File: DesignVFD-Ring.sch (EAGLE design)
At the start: 5 parts, among them J1 NPPN081BFLD-RC, J2 NPPN081BFLD-RC, J3 NPPN081BFLD-RC, J4 NPPN081BFLD-RC

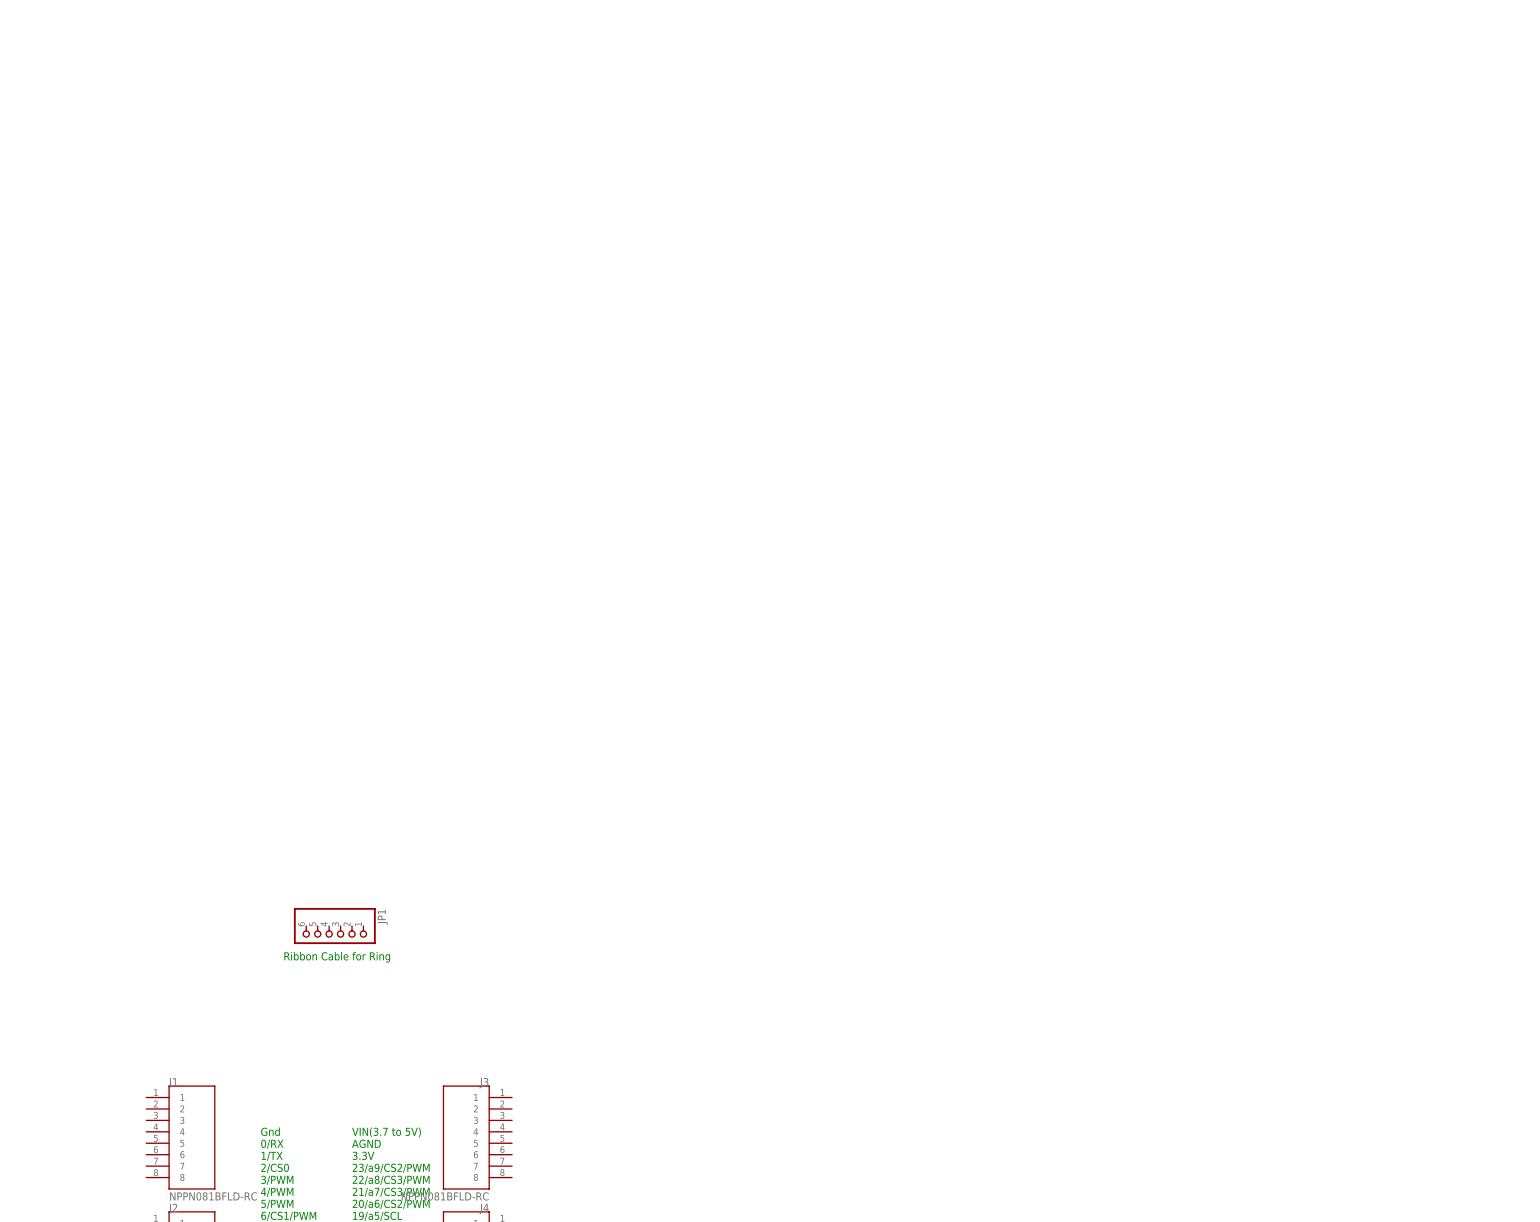
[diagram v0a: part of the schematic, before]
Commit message: downloaded some spreadsheets, added most parts, finished ignition input
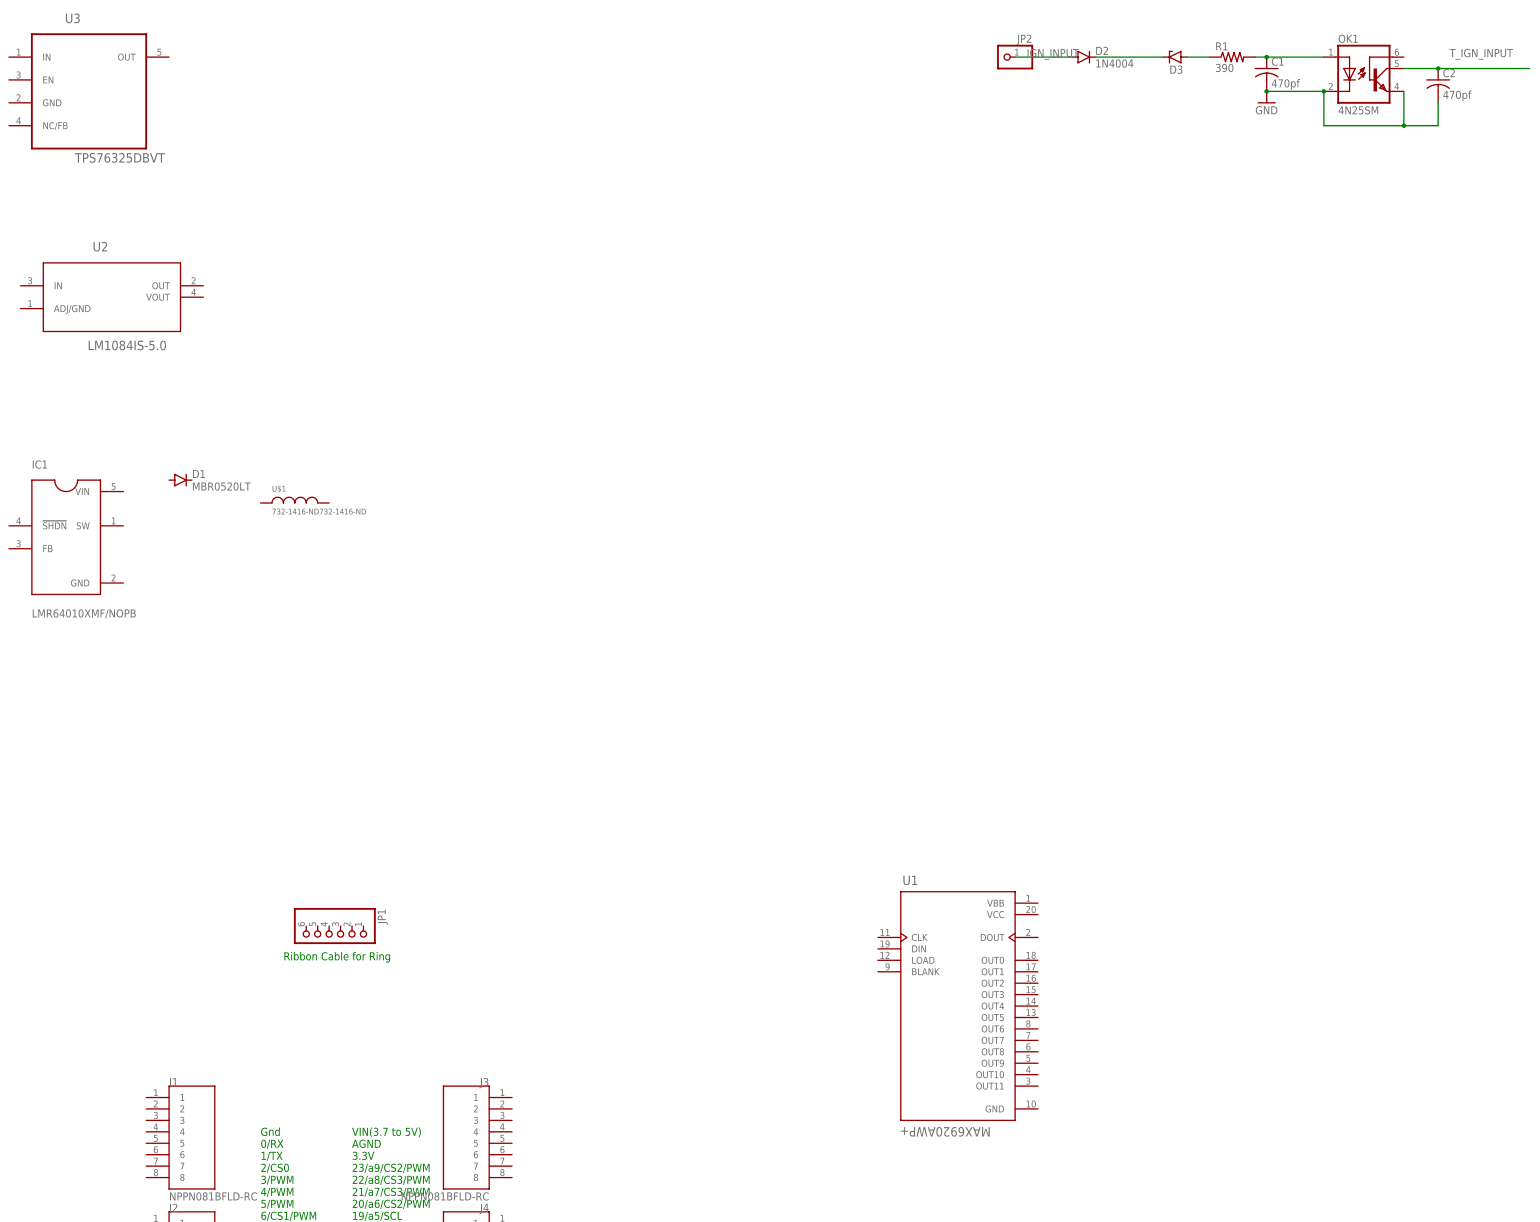
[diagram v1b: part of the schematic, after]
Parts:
- added C1, C2: 470pf, rcl:C-USC0805
- added D1: MBR0520LT, diode:MBR0520LT
- added D2: 1N4004, diode:1N4004
- added D3: (no value), diode:ZENER-DIODEDO41Z10
- added IC1: LMR64010XMF/NOPB, LMR64010XMF_NOPB:LMR64010XMF/NOPB
- added JP2: (no value), pinhead:PINHD-1X1
- added OK1: 4N25SM, 4N25SM:4N25SM
- added R1: 390, rcl:R-US_R0805
- added U$1: 732-1416-ND732-1416-ND, FormE:732-1416-ND732-1416-ND
- added U1: MAX6920AWP+, MAX6920AWP_:MAX6920AWP+
- added U2: LM1084IS-5.0, LM1084IS-5.0:LM1084IS-5.0
- added U3: TPS76325DBVT, TPS76325DBVT:TPS76325DBVT
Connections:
- new net GND: C1.2, C2.2, OK1.C, OK1.EMI
- new net IGN_INPUT: D2.A, JP2.1
- new net N$2: D2.C, D3.C
- new net N$3: D3.A, R1.1
- new net N$4: C1.1, OK1.A, R1.2
- new net T_IGN_INPUT: C2.1, OK1.COL

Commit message: Added IVL2/7-5
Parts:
- added C3, C4, C5, C6: 1uF, rcl:C-USC0805
- added C7: 120pf, rcl:C-USC0805
- added IC2: LM340S-05, linear:LM340S-05
- added R2: PDV-P8103, PDV-P8103:PDV-P8103
- added R3: 10k, rcl:R-US_R0805
- added R4, R5: 0, rcl:R-US_R0805
- added R6: 11k, rcl:R-US_R0805
- added R7: 205k, rcl:R-US_R0805
- added U$2: IVL2-7/5, FormE:IVL2-7/5
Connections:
- new net +12V: IC1.!SHDN, IC1.VIN, IC2.VO, U$1.P$2
- new net +15V: C3.1, C6.1, IC2.VI, U2.IN
- new net +24V: C7.1, D1.C, R7.1, U1.VBB
- new net +3V3: J3.3, R3.2
- new net +5V: C4.1, J3.1, R5.2, U1.VCC, U2.OUT, U3.IN
- new net N$1: R4.2, R5.1, U3.EN
- new net N$10: U$2.MIDDLE, U1.OUT3
- new net N$11: U$2.LOWERLEFT, U1.OUT4
- new net N$12: U$2.LOWERRIGHT, U1.OUT5
- new net N$13: U$2.LOWER, U1.OUT6
- new net N$14: U$2.GRID1, U1.OUT7
- new net N$15: U$2.GRID2, U1.OUT8
- new net N$16: U$2.GRID4, U1.OUT9
- new net N$17: U$2.GRID5, U1.OUT10
- new net N$5: U$2.TOPSEGMENT, U1.OUT0
- new net N$6: D1.A, IC1.SW, U$1.P$1
- new net N$7: C7.2, IC1.FB, R6.2, R7.2
- new net N$8: U$2.TOPLEFT, U1.OUT1
- new net N$9: U$2.TOPRIGHT, U1.OUT2
- new net T_HEATER_CTL: R4.1
- new net T_LIGHT_INPUT: R2.2, R3.1
- new net V+: C5.1, U$2.FILLAMENT2, U3.OUT
- net GND: now also C3.2, C4.2, C5.2, C6.2, IC1.GND, IC2.GND, J1.1, R2.1, R6.1, U$2.FILLAMENT1, U1.GND, U2.ADJ/GND, U3.GND
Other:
- note added: "12V to 24V"
- note added: "5V to 2.5V"
- note added: "Batt to 12V"
- note added: "Batt to 5V"
- note added: "TODO sort Caps"
- moved on the sheet: D1, U$1

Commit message: Initial Schematic complete
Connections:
- new net T_BLANK: J3.4, U1.BLANK
- new net T_CS2: J1.5, U1.LOAD
- new net T_MOSI: J2.5, JP1.4
- new net T_MOSI2: J1.4, U1.DIN
- new net T_SCK: J4.6, JP1.6
- new net T_SCK2: J1.3, U1.CLK
- net +3V3: now also U1.VCC
- net +5V: now also JP1.2; no longer U1.VCC
- net GND: now also J3.2, JP1.1, JP1.3, JP1.5
- net T_IGN_INPUT: now also J1.8
- net T_LIGHT_INPUT: now also J4.4
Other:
- note added: "IVL2-7/5 VFD Display and driver"
- note added: "Ignition coil trigger"
- note added: "Light Sensor"
- moved on the sheet: JP1, R2, R3
